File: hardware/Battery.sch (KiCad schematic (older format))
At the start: 10 parts

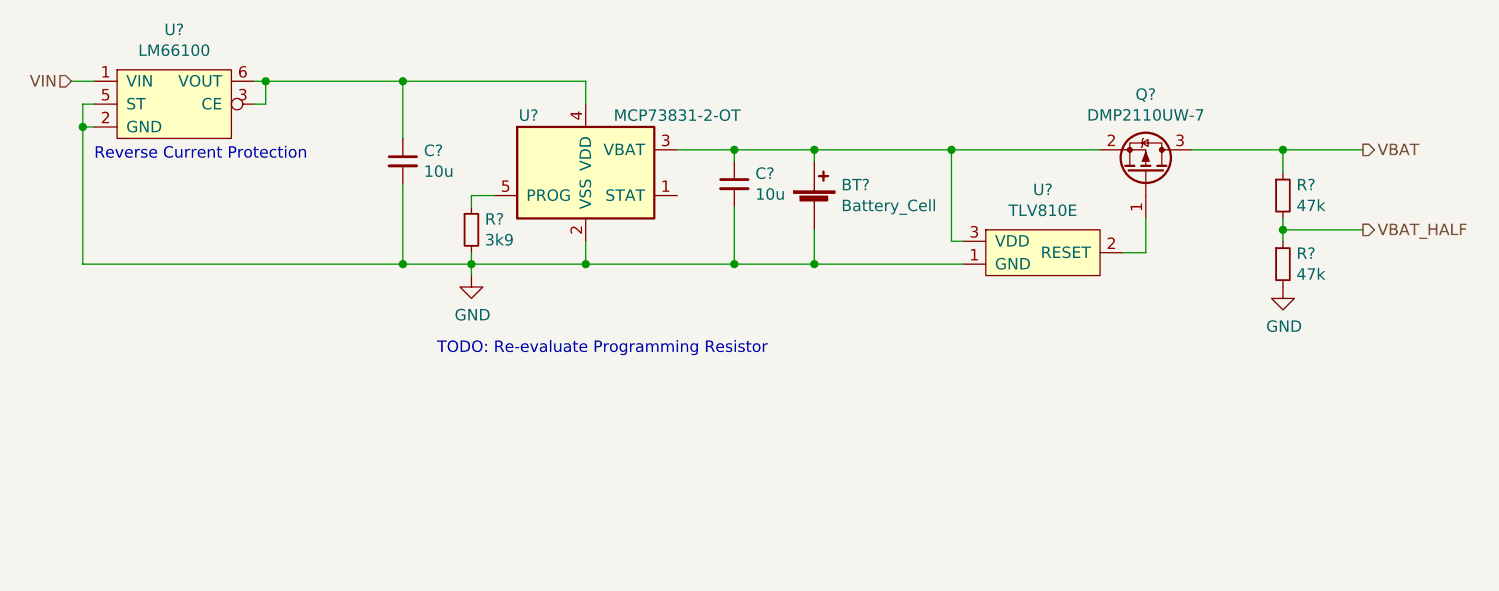
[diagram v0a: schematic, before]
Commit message: schematic should be done, pcb is next
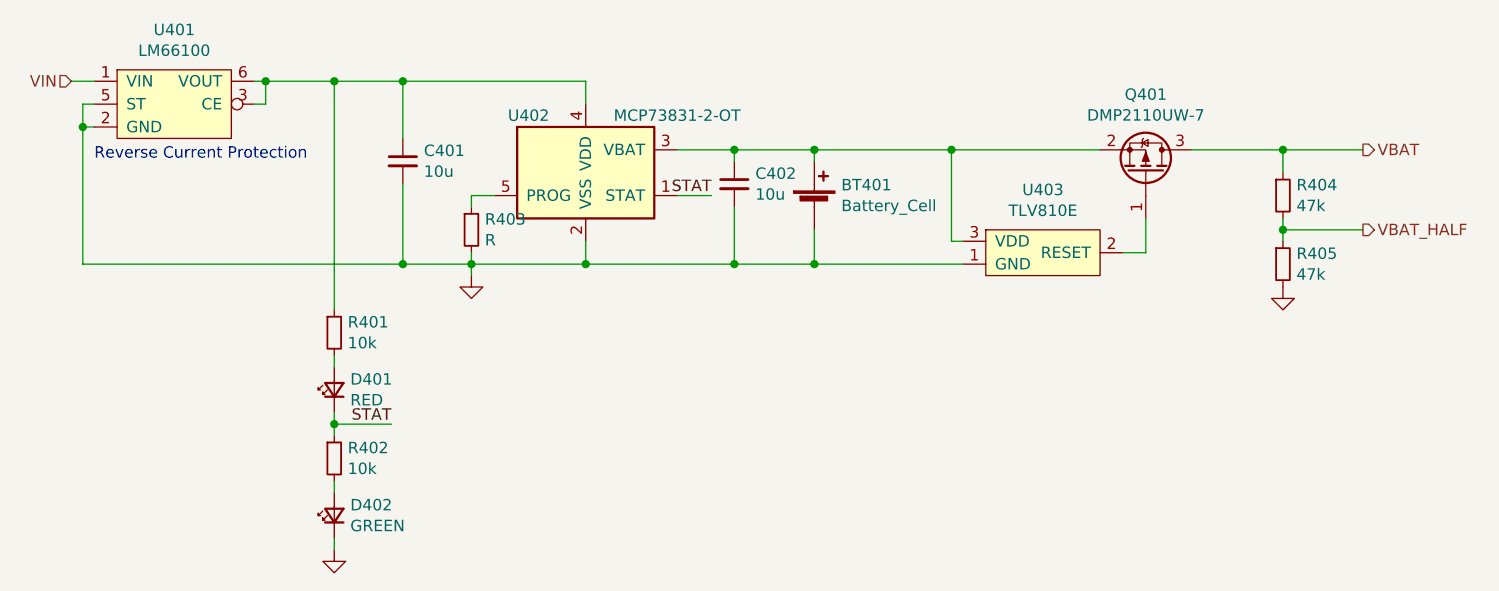
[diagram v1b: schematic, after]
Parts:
- added D401: RED, LED_SMD:LED_0603_1608Metric_Pad1.05x0.95mm_HandSolder, symbol Device:LED_Small
- added D402: GREEN, LED_SMD:LED_0603_1608Metric_Pad1.05x0.95mm_HandSolder, symbol Device:LED_Small
- added R401, R402: 10k, Resistor_SMD:R_0603_1608Metric_Pad1.05x0.95mm_HandSolder, symbol Device:R_Small
- BT401: renamed from BT?; Order https://www.amazon.de/Turnigy-nano-tech-300mah-Solo-Pro-Mod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 -> https://www.amazon.de/YUNIQUE-Deutschland-Quadrocopter-Ersa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
- C401, C402: renamed from C?; Manufacturer (none) -> Samsung Electro-Mechanics; Order https://www.digikey.at/product-detail/de/samsung-electro-me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 -> https://www.mouser.at/ProductDetail/187-CL10B106MQ8NRNC
- Q401: renamed from Q?; Manufacturer (none) -> Diodes Incorporated; Order (none) -> https://www.mouser.at/ProductDetail/Diodes-Incorporated/DMP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
- R403: renamed from R?; value 3k9 -> R; Order https://www.digikey.at/product-detail/de/te-connectivity-pa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 -> (none)
- R404, R405: renamed from R?; Manufacturer (none) -> TE Connectivity / Holsworthy; Order https://www.digikey.at/product-detail/de/te-connectivity-pa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 -> https://www.mouser.at/ProductDetail/279-CRGP0603F47K
- U401: renamed from U?; Manufacturer (none) -> Texas Instruments; Order (none) -> https://www.mouser.at/ProductDetail/595-LM66100DCKR
- U402: renamed from U?; Manufacturer (none) -> Microchip Technology; Order https://www.digikey.at/product-detail/de/microchip-technolo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 -> https://www.mouser.at/ProductDetail/579-MCP73831T-2ACIOT
- gave numbers to parts that had none: 1
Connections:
- net GND: now also D402.1 (K)
- net at C401.1, U401.3 (CE), U401.6 (VOUT)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: now also R401.1
- net STAT: now reaches U402.1 (STAT)
- net STAT: now also D401.1 (K), R402.1
- new net: D401.2 (A), R401.2
- new net: D402.2 (A), R402.2
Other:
- note removed: "TODO: Re-evaluate Programming Resistor"

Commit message: wip hw
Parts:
- C401, C402: footprint Capacitor_SMD:C_0603_1608Metric_Pad1.05x0.95mm_HandSolder -> Capacitor_SMD:C_0805_2012Metric
- D401, D402: footprint LED_SMD:LED_0603_1608Metric_Pad1.05x0.95mm_HandSolder -> LED_SMD:LED_0603_1608Metric
- Q401: footprint Package_TO_SOT_SMD:SOT-323_SC-70_Handsoldering -> Package_TO_SOT_SMD:SOT-323_SC-70
- R401, R402, R403, R404, R405: footprint Resistor_SMD:R_0603_1608Metric_Pad1.05x0.95mm_HandSolder -> Resistor_SMD:R_0603_1608Metric
- U401: footprint lm66100:LM66100DCKT -> watch:Sc70-6
- U403: footprint Package_TO_SOT_SMD:SOT-23_Handsoldering -> Package_TO_SOT_SMD:SOT-23
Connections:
- net GND: now also R402.2; no longer D402.1 (K)
- net STAT: now also D402.2 (A); no longer R402.1
- new net: D402.1 (K), R402.1
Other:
- moved on the sheet: D402, R402
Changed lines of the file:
@@
 F 0 "C401" H 3042 1896 50  0000 L CNN
 F 1 "10u" H 3042 1805 50  0000 L CNN
-F 2 "Capacitor_SMD:C_0603_1608Metric_Pad1.05x0.95mm_HandSolder" H 2950 1850 50  0001 C CNN
+F 2 "Capacitor_SMD:C_0805_2012Metric" H 2950 1850 50  0001 C CNN
 F 3 "https://www.mouser.at/datasheet/2/585/MLCC-1837944.pdf" H 2950 1850 50  0001 C CNN
 F 4 "https://www.mouser.at/ProductDetail/187-CL10B106MQ8NRNC" H 2950 1850 50  0001 C CNN "Order"
@@
 F 0 "C402" H 4492 1996 50  0000 L CNN
 F 1 "10u" H 4492 1905 50  0000 L CNN
-F 2 "Capacitor_SMD:C_0603_1608Metric_Pad1.05x0.95mm_HandSolder" H 4400 1950 50  0001 C CNN
+F 2 "Capacitor_SMD:C_0805_2012Metric" H 4400 1950 50  0001 C CNN
 F 3 "https://www.mouser.at/datasheet/2/585/MLCC-1837944.pdf" H 4400 1950 50  0001 C CNN
 F 4 "https://www.mouser.at/ProductDetail/187-CL10B106MQ8NRNC" H 4400 1950 50  0001 C CNN "Order"
@@
 F 0 "R403" H 3309 2196 50  0000 L CNN
 F 1 "R" H 3309 2105 50  0000 L CNN
-F 2 "Resistor_SMD:R_0603_1608Metric_Pad1.05x0.95mm_HandSolder" H 3250 2150 50  0001 C CNN
+F 2 "Resistor_SMD:R_0603_1608Metric" H 3250 2150 50  0001 C CNN
 F 3 "~" H 3250 2150 50  0001 C CNN
 F 4 "" H 3250 2150 50  0001 C CNN "Order"
@@
 F 0 "Q401" V 6542 1900 50  0000 C CNN
 F 1 "DMP2110UW-7" V 6451 1900 50  0000 C CNN
-F 2 "Package_TO_SOT_SMD:SOT-323_SC-70_Handsoldering" H 6400 2000 50  0001 C CNN
+F 2 "Package_TO_SOT_SMD:SOT-323_SC-70" H 6400 2000 50  0001 C CNN
 F 3 "https://www.diodes.com/assets/Datasheets/DMP2110UW.pdf" H 6200 1900 50  0001 C CNN
 F 4 "Diodes Incorporated" H 6200 1900 50  0001 C CNN "Manufacturer"
@@
 F 0 "U403" H 5750 2525 50  0000 C CNN
 F 1 "TLV810E" H 5750 2434 50  0000 C CNN
-F 2 "Package_TO_SOT_SMD:SOT-23_Handsoldering" H 6150 2950 50  0001 C CNN
+F 2 "Package_TO_SOT_SMD:SOT-23" H 6150 2950 50  0001 C CNN
 F 3 "" H 6150 2950 50  0001 C CNN
 	1    5750 2250
@@
 F 0 "R405" H 6859 2346 50  0000 L CNN
 F 1 "47k" H 6859 2255 50  0000 L CNN
-F 2 "Resistor_SMD:R_0603_1608Metric_Pad1.05x0.95mm_HandSolder" H 6800 2300 50  0001 C CNN
+F 2 "Resistor_SMD:R_0603_1608Metric" H 6800 2300 50  0001 C CNN
 F 3 "https://www.mouser.at/datasheet/2/418/5/NG_DS_9-1773463-9_A-1358566.pdf" H 6800 2300 50  0001 C CNN
 F 4 "https://www.mouser.at/ProductDetail/279-CRGP0603F47K" H 6800 2300 50  0001 C CNN "Order"
@@
 F 0 "R404" H 6859 2046 50  0000 L CNN
 F 1 "47k" H 6859 1955 50  0000 L CNN
-F 2 "Resistor_SMD:R_0603_1608Metric_Pad1.05x0.95mm_HandSolder" H 6800 2000 50  0001 C CNN
+F 2 "Resistor_SMD:R_0603_1608Metric" H 6800 2000 50  0001 C CNN
 F 3 "https://www.mouser.at/datasheet/2/418/5/NG_DS_9-1773463-9_A-1358566.pdf" H 6800 2000 50  0001 C CNN
 F 4 "https://www.mouser.at/ProductDetail/279-CRGP0603F47K" H 6800 2000 50  0001 C CNN "Order"
@@
 F 0 "U401" H 1950 1925 50  0000 C CNN
 F 1 "LM66100" H 1950 1834 50  0000 C CNN
-F 2 "lm66100:LM66100DCKT" H 2300 1850 50  0001 C CNN
+F 2 "watch:Sc70-6" H 2300 1850 50  0001 C CNN
 F 3 "https://www.ti.com/lit/ds/symlink/lm66100.pdf?HQS=dis-mous-null-mousermode-dsf-pf-null-wwe&DCM=yes&ref_url=https%3A%2F%2Fwww.mouser.it%2F&distId=26" H 2300 1850 50  0001 C CNN
 F 4 "Texas Instruments" H 1950 1600 50  0001 C CNN "Manufacturer"
@@
 F 0 "D401" V 2696 2780 50  0000 R CNN
 F 1 "RED" V 2605 2780 50  0000 R CNN
-F 2 "LED_SMD:LED_0603_1608Metric_Pad1.05x0.95mm_HandSolder" V 2650 2850 50  0001 C CNN
+F 2 "LED_SMD:LED_0603_1608Metric" V 2650 2850 50  0001 C CNN
 F 3 "https://www.mouser.at/datasheet/2/216/AA1608SURSK-1951973.pdf" V 2650 2850 50  0001 C CNN
 F 4 "AA1608SURSK" V 2650 2850 50  0001 C CNN "Part Number"
@@
 F 0 "R401" H 2709 2646 50  0000 L CNN
 F 1 "10k" H 2709 2555 50  0000 L CNN
-F 2 "Resistor_SMD:R_0603_1608Metric_Pad1.05x0.95mm_HandSolder" H 2650 2600 50  0001 C CNN
+F 2 "Resistor_SMD:R_0603_1608Metric" H 2650 2600 50  0001 C CNN
 F 3 "~" H 2650 2600 50  0001 C CNN
 F 4 "" H 2650 2600 50  0001 C CNN "Order"
@@
 L Device:R_Small R402
 U 1 1 606121EB
-P 2650 3150
-F 0 "R402" H 2709 3196 50  0000 L CNN
-F 1 "10k" H 2709 3105 50  0000 L CNN
-F 2 "Resistor_SMD:R_0603_1608Metric_Pad1.05x0.95mm_HandSolder" H 2650 3150 50  0001 C CNN
-F 3 "~" H 2650 3150 50  0001 C CNN
-F 4 "" H 2650 3150 50  0001 C CNN "Order"
-	1    2650 3150
+P 2650 3400
+F 0 "R402" H 2709 3446 50  0000 L CNN
+F 1 "10k" H 2709 3355 50  0000 L CNN
+F 2 "Resistor_SMD:R_0603_1608Metric" H 2650 3400 50  0001 C CNN
+F 3 "~" H 2650 3400 50  0001 C CNN
+F 4 "" H 2650 3400 50  0001 C CNN "Order"
+	1    2650 3400
 	1    0    0    -1
 $EndComp
@@
 L Device:LED_Small D402
 U 1 1 606121F3
-P 2650 3400
-F 0 "D402" V 2696 3330 50  0000 R CNN
-F 1 "GREEN" V 2605 3330 50  0000 R CNN
-F 2 "LED_SMD:LED_0603_1608Metric_Pad1.05x0.95mm_HandSolder" V 2650 3400 50  0001 C CNN
-F 3 "https://www.mouser.at/datasheet/2/216/AA1608CGSK-1951957.pdf" V 2650 3400 50  0001 C CNN
-F 4 "Kingbright" H 2650 3400 50  0001 C CNN "Manufacturer"
-F 5 "AA1608CGSK" H 2650 3400 50  0001 C CNN "Part Number"
-F 6 "https://www.mouser.at/ProductDetail/Kingbright/AA1608CGSK?qs=%2Fha2pyFadujroVvVMWEuOp8b2ZvB17TZCtvrJxnHY68n8r1EECXbcw%3D%3D" H 2650 3400 50  0001 C CNN "Order"
-	1    2650 3400
+P 2650 3150
+F 0 "D402" V 2696 3080 50  0000 R CNN
+F 1 "GREEN" V 2605 3080 50  0000 R CNN
+F 2 "LED_SMD:LED_0603_1608Metric" V 2650 3150 50  0001 C CNN
+F 3 "https://www.mouser.at/datasheet/2/216/AA1608CGSK-1951957.pdf" V 2650 3150 50  0001 C CNN
+F 4 "Kingbright" H 2650 3150 50  0001 C CNN "Manufacturer"
+F 5 "AA1608CGSK" H 2650 3150 50  0001 C CNN "Part Number"
+F 6 "https://www.mouser.at/ProductDetail/Kingbright/AA1608CGSK?qs=%2Fha2pyFadujroVvVMWEuOp8b2ZvB17TZCtvrJxnHY68n8r1EECXbcw%3D%3D" H 2650 3150 50  0001 C CNN "Order"
+	1    2650 3150
 	0    -1   -1   0
 $EndComp

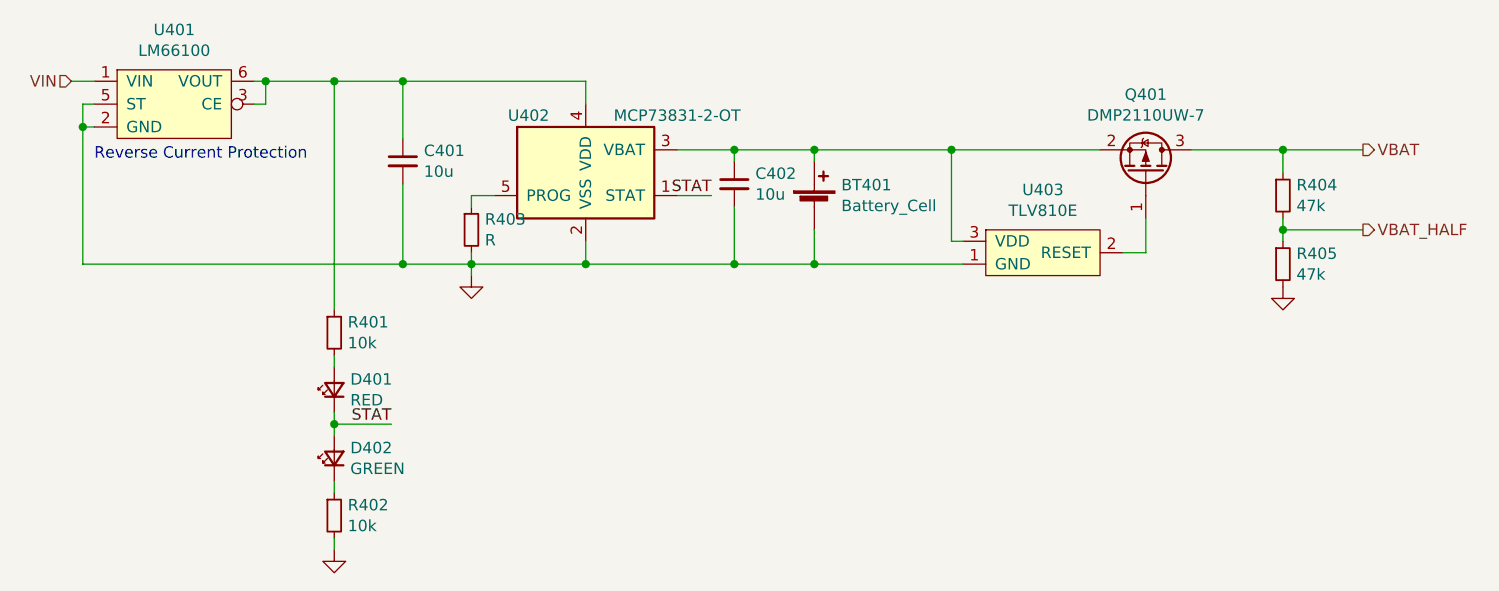
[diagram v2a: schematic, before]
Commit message: calc current consumption
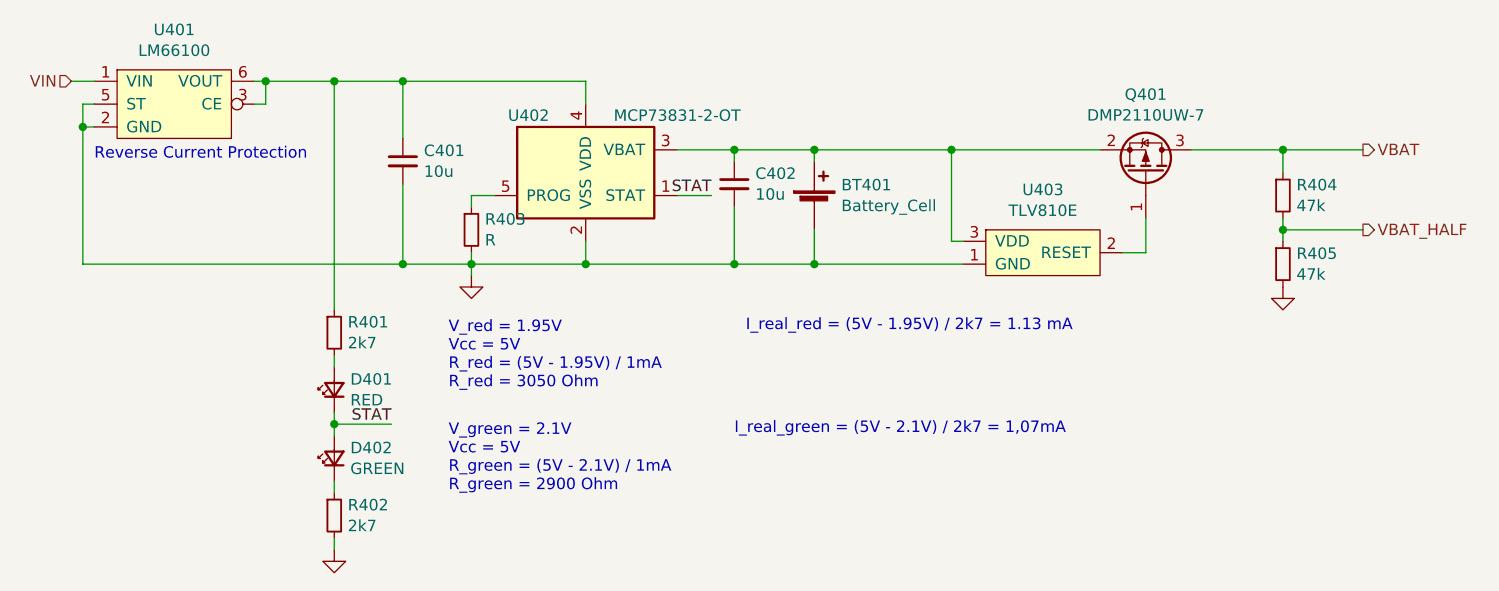
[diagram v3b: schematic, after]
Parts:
- R401, R402: value 10k -> 2k7
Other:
- note added: "I_real_green = (5V - 2.1V) / 2k7 = 1,07mA"
- note added: "I_real_red = (5V - 1.95V) / 2k7 = 1.13 mA"
- note added: "V_green = 2.1V\nVcc = 5V\nR_green = (5V - 2.1V) / 1mA\nR_green = 2900 Ohm"
- note added: "V_red = 1.95V\nVcc = 5V\nR_red = (5V - 1.95V) / 1mA\nR_red = 3050 Ohm\n"
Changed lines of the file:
@@
 P 2650 2600
 F 0 "R401" H 2709 2646 50  0000 L CNN
-F 1 "10k" H 2709 2555 50  0000 L CNN
+F 1 "2k7" H 2709 2555 50  0000 L CNN
 F 2 "Resistor_SMD:R_0603_1608Metric" H 2650 2600 50  0001 C CNN
 F 3 "~" H 2650 2600 50  0001 C CNN
@@
 P 2650 3400
 F 0 "R402" H 2709 3446 50  0000 L CNN
-F 1 "10k" H 2709 3355 50  0000 L CNN
+F 1 "2k7" H 2709 3355 50  0000 L CNN
 F 2 "Resistor_SMD:R_0603_1608Metric" H 2650 3400 50  0001 C CNN
 F 3 "~" H 2650 3400 50  0001 C CNN
@@
 Wire Wire Line
 	2650 1500 2950 1500
+Text Notes 3150 2850 0    50   ~ 0
+V_red = 1.95V\nVcc = 5V\nR_red = (5V - 1.95V) / 1mA\nR_red = 3050 Ohm\n
+Text Notes 3150 3300 0    50   ~ 0
+V_green = 2.1V\nVcc = 5V\nR_green = (5V - 2.1V) / 1mA\nR_green = 2900 Ohm
+Text Notes 4450 2600 0    50   ~ 0
+I_real_red = (5V - 1.95V) / 2k7 = 1.13 mA
+Text Notes 4400 3050 0    50   ~ 0
+I_real_green = (5V - 2.1V) / 2k7 = 1,07mA
 $EndSCHEMATC

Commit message: calculate current consumption
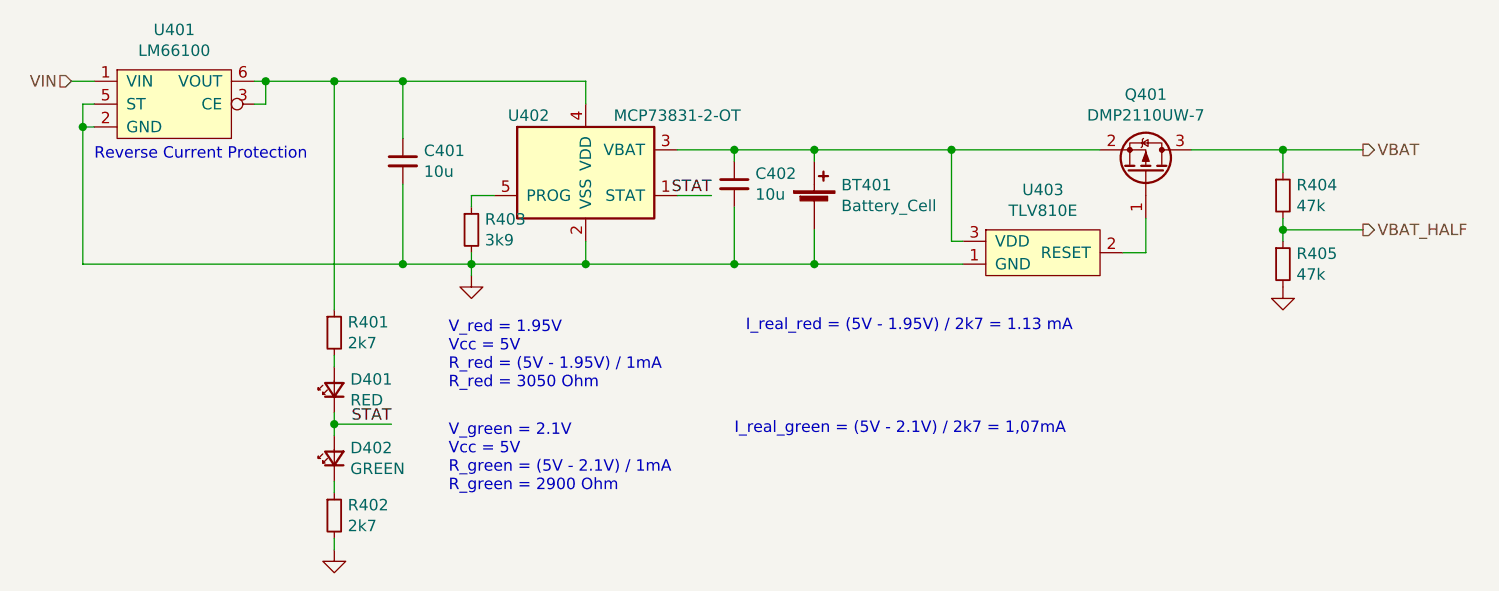
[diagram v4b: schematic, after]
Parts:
- R403: value R -> 3k9
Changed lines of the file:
@@
 AR Path="/6063DAC2/60645BB5" Ref="R403"  Part="1"
 F 0 "R403" H 3309 2196 50  0000 L CNN
-F 1 "R" H 3309 2105 50  0000 L CNN
+F 1 "3k9" H 3309 2105 50  0000 L CNN
 F 2 "Resistor_SMD:R_0603_1608Metric" H 3250 2150 50  0001 C CNN
 F 3 "~" H 3250 2150 50  0001 C CNN

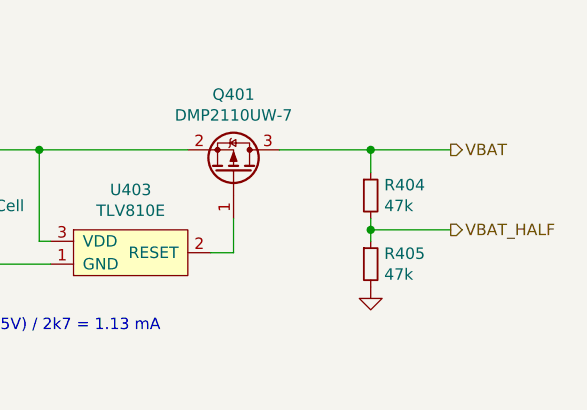
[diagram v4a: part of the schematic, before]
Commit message: added powerflags
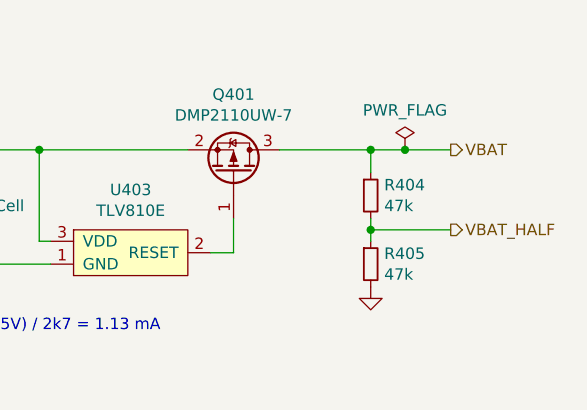
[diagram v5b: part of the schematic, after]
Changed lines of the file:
@@
 	6800 1800 6800 1900
 Wire Wire Line
-	6800 1800 7150 1800
+	6800 1800 6950 1800
 Connection ~ 6800 1800
 Text HLabel 7150 2150 2    50   Output ~ 0
@@
 Text Notes 4400 3050 0    50   ~ 0
 I_real_green = (5V - 2.1V) / 2k7 = 1,07mA
+$Comp
+L power:PWR_FLAG #FLG0105
+U 1 1 606AB429
+P 6950 1800
+F 0 "#FLG0105" H 6950 1875 50  0001 C CNN
+F 1 "PWR_FLAG" H 6950 1973 50  0000 C CNN
+F 2 "" H 6950 1800 50  0001 C CNN
+F 3 "~" H 6950 1800 50  0001 C CNN
+	1    6950 1800
+	1    0    0    -1
+$EndComp
+Connection ~ 6950 1800
+Wire Wire Line
+	6950 1800 7150 1800
 $EndSCHEMATC
